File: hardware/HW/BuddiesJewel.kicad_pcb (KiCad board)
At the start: 2 copper layers, 26 parts, among them CON1 AVR-ISP6, CON2 ANTENNE, P1 ALIM, U1 ATTINY25-P, U2 RF430CL330H

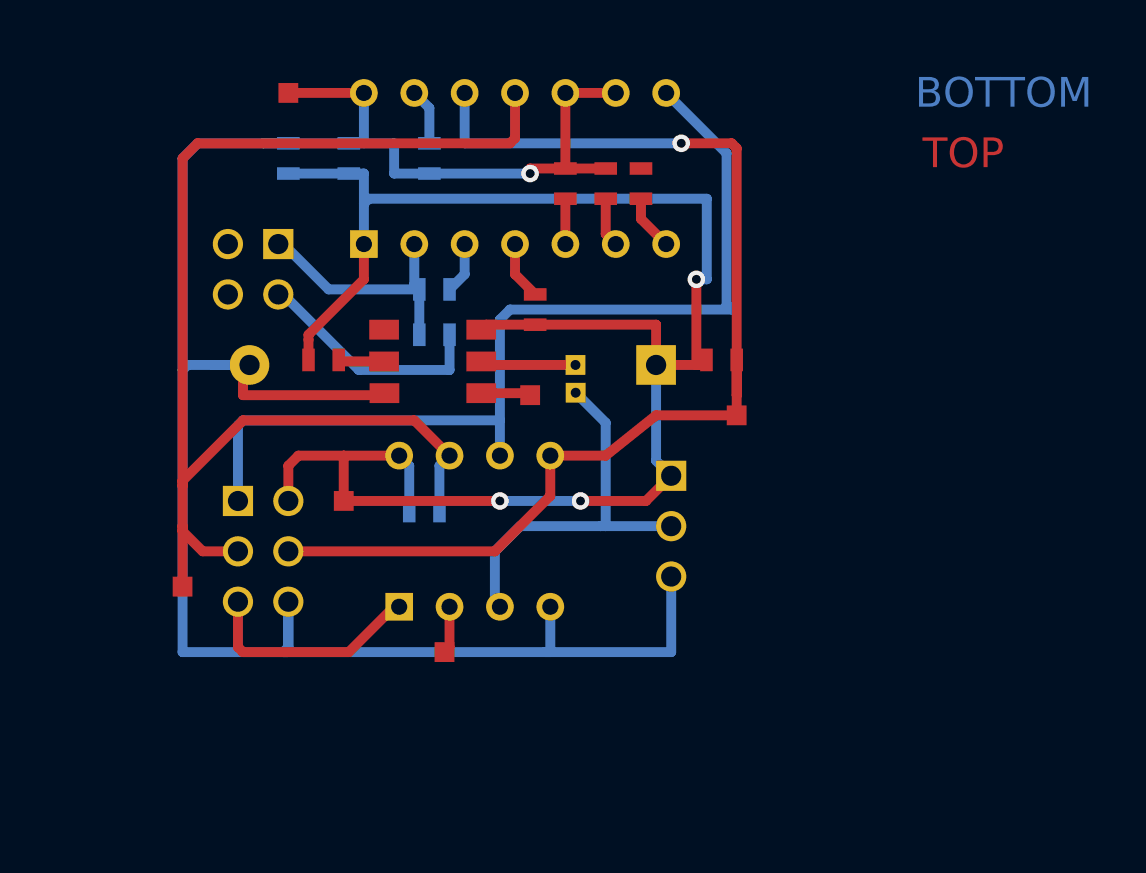
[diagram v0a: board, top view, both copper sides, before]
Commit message: PCB_v1.3
- fix some bugs (missed connection, bad nodes...)
- remove some useless vias
- redo the antenna (just in case where that could work ;)
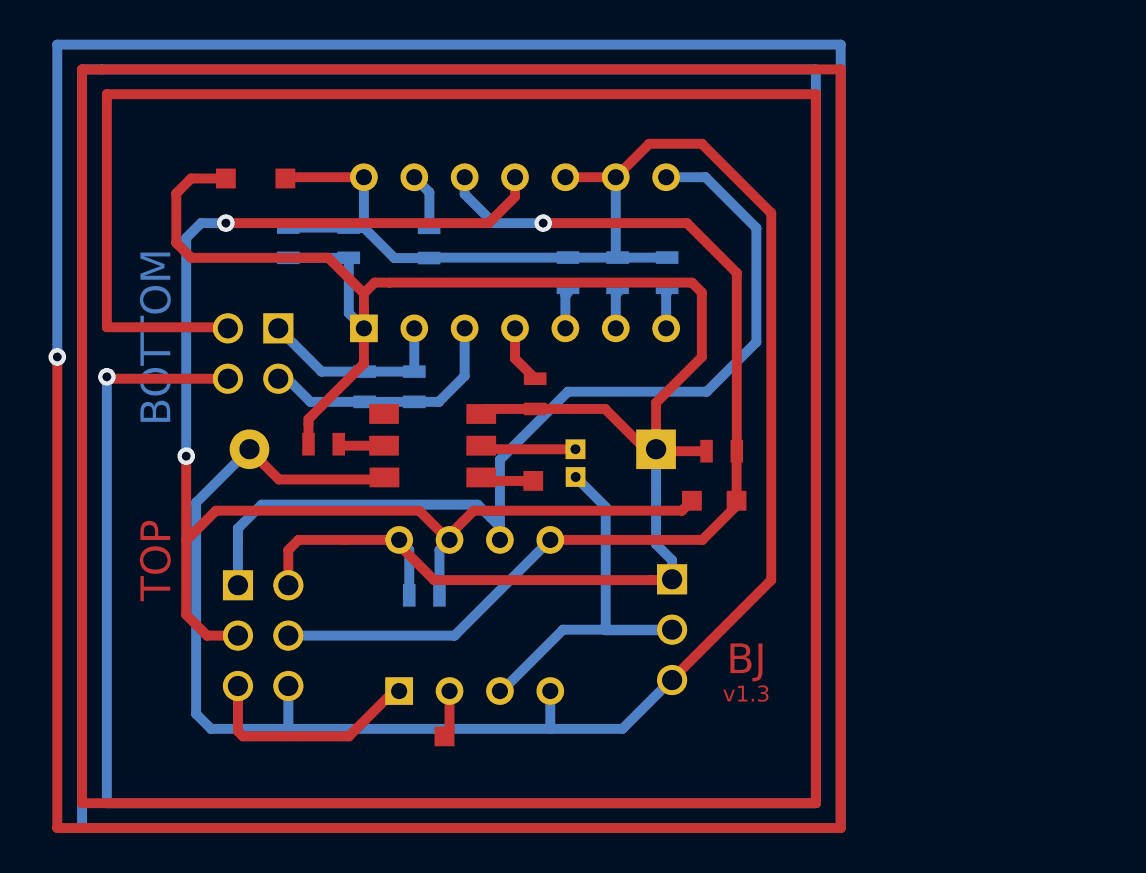
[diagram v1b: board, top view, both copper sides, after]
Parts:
- R4, R5, R6: moved to B.Cu
- moved PT3 26.0 mm to (77.5, 48.2)
- moved D2 5.22 mm to (76.5, 54.8)
- moved C4 5.01 mm to (63.5, 42.5), turned to 270 degrees
- moved R6 4.68 mm to (76.2, 36.8)
- moved R2 4.60 mm to (79.0, 45.8)
- moved R5 4.53 mm to (73.8, 36.8)
- moved R4 4.49 mm to (71.2, 36.8)
- moved C5 4.39 mm to (61.0, 42.5), turned to 270 degrees
- moved PT5 4.33 mm to (69.5, 47.2)
- moved PT4 4.31 mm to (79.8, 48.2)
- moved C3 4.26 mm to (64.2, 35.2)
- moved U2 4.25 mm to (68.6, 35.7)
- moved C1 4.25 mm to (57.1, 35.2)
- moved C2 4.25 mm to (60.2, 35.2)
- moved CON1 4.25 mm to (55.9, 55.0)
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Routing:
- net N-0000016: track 0.00 -> 611.6 mm, vias 0 -> 2
- net +3.3V: track 90.1 -> 103.4 mm, vias 3 -> 0
- net GND: track 112.9 -> 121.0 mm, vias 1 -> 0
- net /SCL/SCK: track 63.2 -> 71.2 mm, vias 0 -> 2
- net /SDA/MOSI: track 58.1 -> 53.3 mm
- net /ANT1: track 12.1 -> 9.94 mm
- net /LED_DI: track 19.7 -> 21.6 mm
- net /ANT2: track 14.0 -> 12.8 mm
- net N-000008: track 2.81 -> 1.81 mm
- net N-000009: track 2.50 -> 1.83 mm
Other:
- board text added: "BJ"
- board text added: "v1.3"

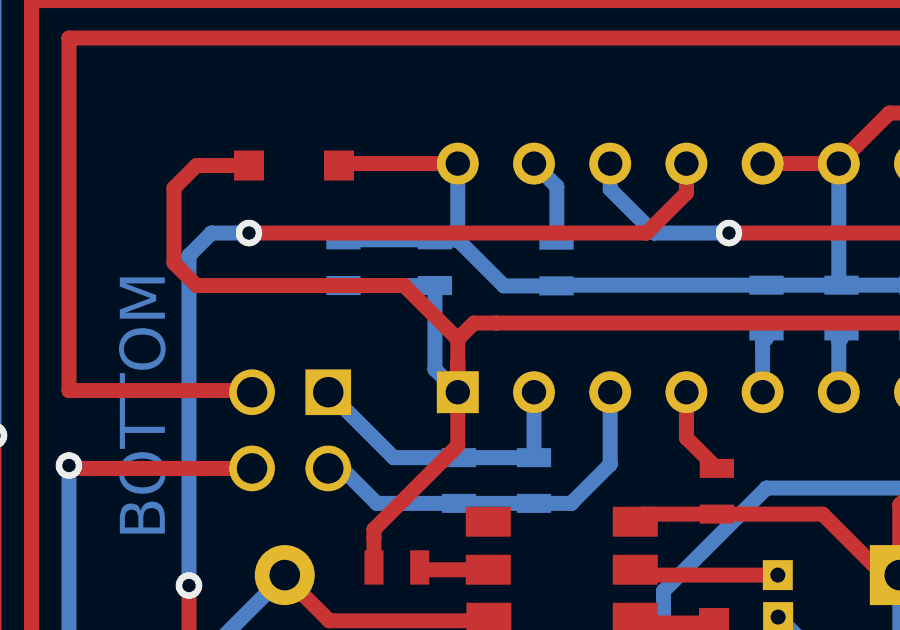
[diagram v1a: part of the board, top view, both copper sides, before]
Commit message: PCB_v1.3.1
(minor) move C2 to the good position
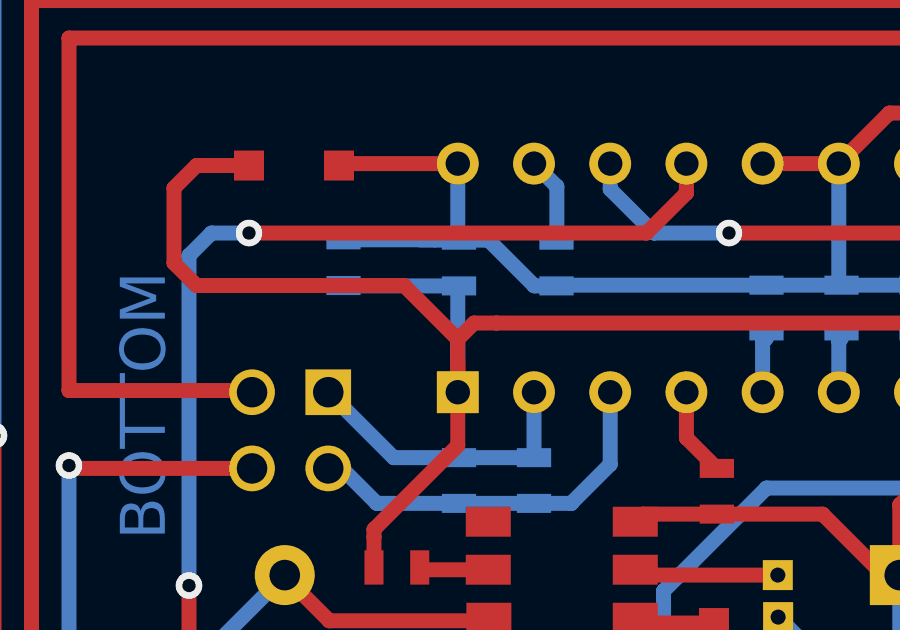
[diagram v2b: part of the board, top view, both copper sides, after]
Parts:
- moved C2 0.80 mm to (61.0, 35.2)
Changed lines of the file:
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@@
     (links 55)
     (no_connects 0)
-    (area 31.750001 15.400001 98.499999 68.45)
+    (area 32.000001 17.25 98.499999 72.45)
     (thickness 1.6)
     (drawings 21)
-    (tracks 193)
+    (tracks 195)
     (zones 0)
     (modules 26)
@@
   (title_block
     (title "Proto BuddiesJewel")
-    (rev 1.3)
+    (rev 1.3.1)
     (company BuddiesProjects)
   )
@@
   )
   (module SM0603_Capa (layer Dessous.Cu)
-    (at 60.198 35.238 270)
+    (at 61 35.25 270)
     (attr smd)
     (fp_text reference C2 (at 0 0 540) (layer Dessous.SilkS)
@@
   (target plus (at 81 31.25) (size 1) (width 0.1) (layer Contours.Ci))
   (target plus (at 50.5 31.25) (size 1) (width 0.1) (layer Contours.Ci))
+  (segment (start 61 36.012) (end 57.162 36.012) (width 0.5) (layer Dessous.Cu) (net 1))
+  (segment (start 57.162 36.012) (end 57.15 36) (width 0.5) (layer Dessous.Cu) (net 1))
+  (segment (start 60.96 39.556) (end 60.96 36.052) (width 0.5) (layer Dessous.Cu) (net 1))
+  (segment (start 60.96 36.052) (end 61 36.012) (width 0.5) (layer Dessous.Cu) (net 1))
   (segment (start 76.5 52.21) (end 76.5 51.25) (width 0.5) (layer Dessous.Cu) (net 1))
   (segment (start 75.692 50.442) (end 75.692 45.652) (width 0.5) (layer Dessous.Cu) (net 1))
   (segment (start 76.5 51.25) (end 75.692 50.442) (width 0.5) (layer Dessous.Cu) (net 1))
-  (segment (start 60.198 36) (end 60.198 38.794) (width 0.5) (layer Dessous.Cu) (net 1))
-  (segment (start 60.198 38.794) (end 60.96 39.556) (width 0.5) (layer Dessous.Cu) (net 1))
   (segment (start 62.25 37.25) (end 61.5 37.25) (width 0.5) (layer Dessus.Cu) (net 1))
   (segment (start 75.692 43.308) (end 78 41) (width 0.5) (layer Dessus.Cu) (net 1))
@@
   (segment (start 58.166 44.128) (end 60.96 41.334) (width 0.5) (layer Dessus.Cu) (net 1))
   (segment (start 58.166 44.382) (end 58.166 44.128) (width 0.5) (layer Dessus.Cu) (net 1))
-  (segment (start 57.15 36) (end 60.198 36) (width 0.5) (layer Dessous.Cu) (net 1))
   (segment (start 63.246 53.018) (end 63.246 50.732) (width 0.5) (layer Dessous.Cu) (net 1))
   (segment (start 63.246 50.732) (end 62.738 50.224) (width 0.5) (layer Dessous.Cu) (net 1))
@@
   (segment (start 54.61 49.64) (end 55.804 48.446) (width 0.5) (layer Dessous.Cu) (net 4))
   (via (at 54.61 52.51) (size 0.889) (layers Dessus.Cu Dessous.Cu) (net 4))
-  (segment (start 76.5 54.75) (end 71 54.75) (width 0.5) (layer Dessous.Cu) (net 5) (status 400000))
-  (segment (start 67.906 57.844) (end 67.818 57.844) (width 0.5) (layer Dessous.Cu) (net 5) (status C00000))
-  (segment (start 71 54.75) (end 67.906 57.844) (width 0.5) (layer Dessous.Cu) (net 5) (status 800000))
+  (segment (start 76.5 54.75) (end 71 54.75) (width 0.5) (layer Dessous.Cu) (net 5))
+  (segment (start 67.906 57.844) (end 67.818 57.844) (width 0.5) (layer Dessous.Cu) (net 5))
+  (segment (start 71 54.75) (end 67.906 57.844) (width 0.5) (layer Dessous.Cu) (net 5))
   (segment (start 71.638 47.052) (end 73.152 48.566) (width 0.5) (layer Dessous.Cu) (net 5))
   (segment (start 73.152 48.566) (end 73.152 54.78) (width 0.5) (layer Dessous.Cu) (net 5))
@@
   (segment (start 64.77 53.018) (end 64.77 50.732) (width 0.5) (layer Dessous.Cu) (net 7))
   (segment (start 64.77 50.732) (end 65.278 50.224) (width 0.5) (layer Dessous.Cu) (net 7))
-  (segment (start 79.75 48.25) (end 79.75 48.5) (width 0.5) (layer Dessus.Cu) (net 8) (status C00000))
-  (segment (start 79.75 48.5) (end 78.026 50.224) (width 0.5) (layer Dessus.Cu) (net 8) (status 400000))
+  (segment (start 79.75 48.25) (end 79.75 48.5) (width 0.5) (layer Dessus.Cu) (net 8))
+  (segment (start 79.75 48.5) (end 78.026 50.224) (width 0.5) (layer Dessus.Cu) (net 8))
   (segment (start 79.75 48.25) (end 79.75 45.762) (width 0.5) (layer Dessus.Cu) (net 8))
   (segment (start 79.75 45.762) (end 79.762 45.75) (width 0.5) (layer Dessus.Cu) (net 8))
@@
   (segment (start 57.15 55.05) (end 65.532 55.05) (width 0.5) (layer Dessous.Cu) (net 8))
   (segment (start 65.532 55.05) (end 70.358 50.224) (width 0.5) (layer Dessous.Cu) (net 8))
-  (segment (start 64.25 36.012) (end 62.496 36.012) (width 0.5) (layer Dessous.Cu) (net 9))
-  (segment (start 62.496 36.012) (end 60.96 34.476) (width 0.5) (layer Dessous.Cu) (net 9))
+  (segment (start 64.25 36.012) (end 63.512 36.012) (width 0.5) (layer Dessous.Cu) (net 9))
+  (segment (start 61.988 34.488) (end 61 34.488) (width 0.5) (layer Dessous.Cu) (net 9))
+  (segment (start 63.512 36.012) (end 61.988 34.488) (width 0.5) (layer Dessous.Cu) (net 9))
   (segment (start 60.96 34.476) (end 60.198 34.476) (width 0.5) (layer Dessous.Cu) (net 9))
   (segment (start 71.25 35.988) (end 64.274 35.988) (width 0.5) (layer Dessous.Cu) (net 9))

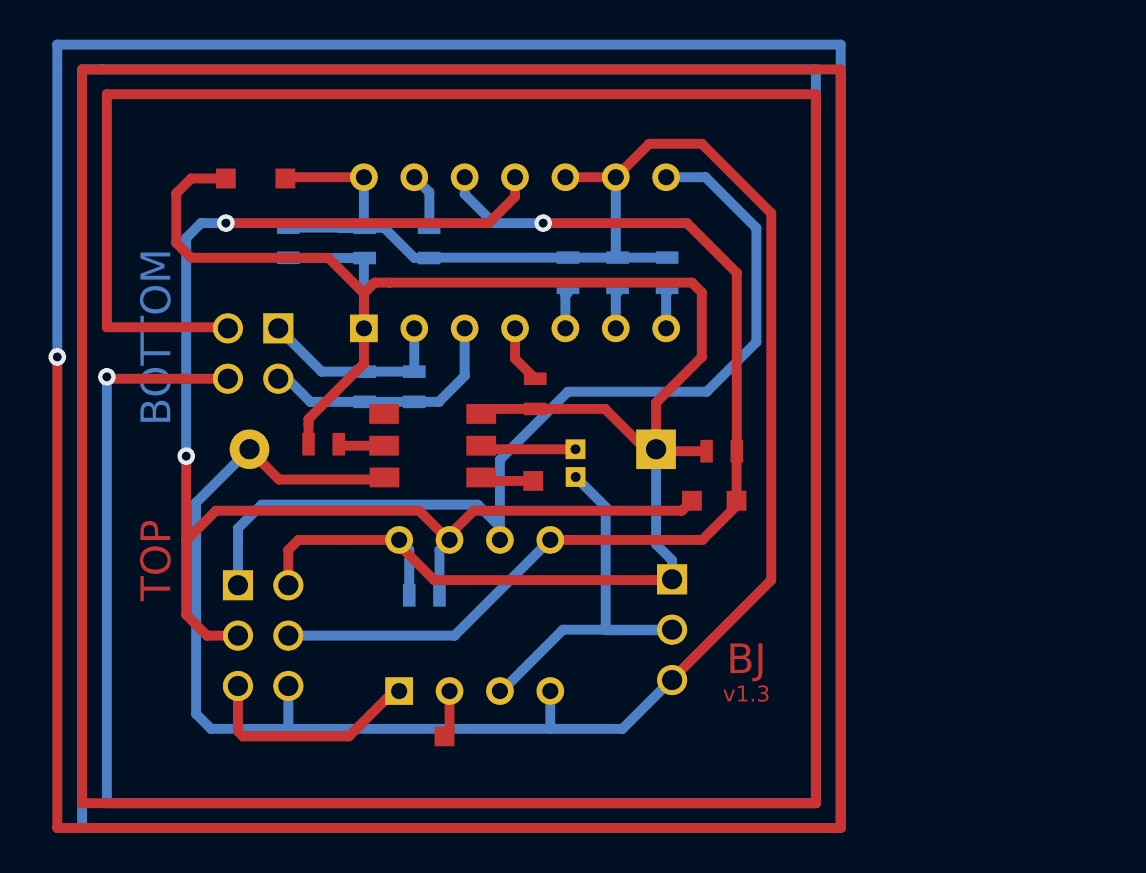
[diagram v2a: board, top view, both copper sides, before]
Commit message: PCB_v1.4
**will be used for our first etch**

- increase track width to .8mm (antenna tracks still in .5mm)
- remove the LED_DI jumper then replaced with a 0 ohm resistor (freed space)
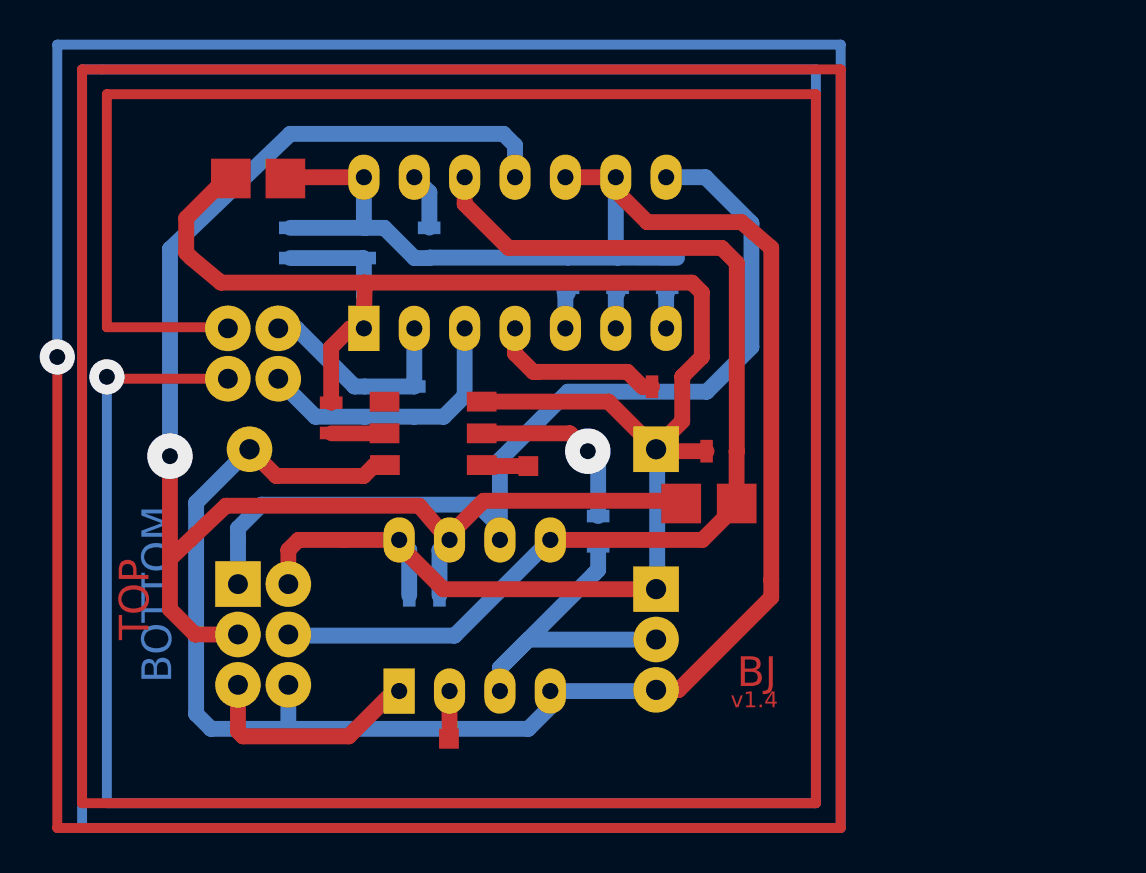
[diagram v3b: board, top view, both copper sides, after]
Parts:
- removed D1: WS2812, WS2812
- removed D2: EXT_LED, PIN_ARRAY_3X1
- removed JP1: JUMPER, Jumper
- added CON3: EXT_LED, PIN_ARRAY_3X1, F.Cu at (75.7, 55.2)
- added R8: zero R, SM0603_Resistor, B.Cu at (72.8, 49.8)
- added U3: WS2812, WS2812, F.Cu at (62.0, 43.2)
- U1: footprint DIP-8__300 -> DIP-8__300_ELL
- U2: footprint DIP-14__300 -> DIP-14__300_ELL
- moved PT1 21.3 mm to (54.2, 32.0)
- moved R3 6.66 mm to (76.2, 42.5), turned to 0 degrees
- moved R7 1.38 mm to (59.3, 44.1), turned to 270 degrees
- moved PT5 0.79 mm to (69.2, 46.5)
- moved C4 0.75 mm to (63.5, 43.2)
- moved C5 0.75 mm to (61.0, 43.2)
- moved PT3 0.56 mm to (77.0, 48.4)
- moved PT6 0.26 mm to (65.2, 60.2)
- moved PT4 0.14 mm to (79.8, 48.4)
- moved C1 0.10 mm to (57.2, 35.2)
- moved CON1 0.06 mm to (55.9, 55.0)
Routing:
- net N-0000010: track 0.00 -> 9.21 mm, vias 0 -> 1
- net N-000006: track 2.96 -> 8.90 mm
- net N-000003 (its old number): track 4.83 -> 0.00 mm
- net /SCL/SCK: track 71.2 -> 75.8 mm, vias 2 -> 1
- net GND: track 120.9 -> 117.1 mm
- net +3.3V: track 103.9 -> 100.2 mm
- net /LED_DI: track 21.6 -> 17.9 mm
- net /ANT2: track 12.8 -> 14.1 mm
- net /ANT1: track 9.94 -> 11.0 mm
- net /SDA/MOSI: track 53.3 -> 53.9 mm, vias 1 -> 0
- net /IT/MISO: track 48.5 -> 48.3 mm, vias 1 -> 0
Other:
- net class Default: trace_width 0.5 -> 0.8; via_dia 0.889 -> 2.3; via_drill 0.635 -> 0.8
- board text added: "v1.4"
- board text removed: "v1.3"
